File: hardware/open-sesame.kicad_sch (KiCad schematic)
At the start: 20 parts, among them J1 Barrel_Jack_Switch, J2 Screw_Terminal_01x02, J3 Screw_Terminal_01x04, J4 Screw_Terminal_01x03, J5 Screw_Terminal_01x03, J6 Qwiic_RA, U1 PC817, U2 PC817

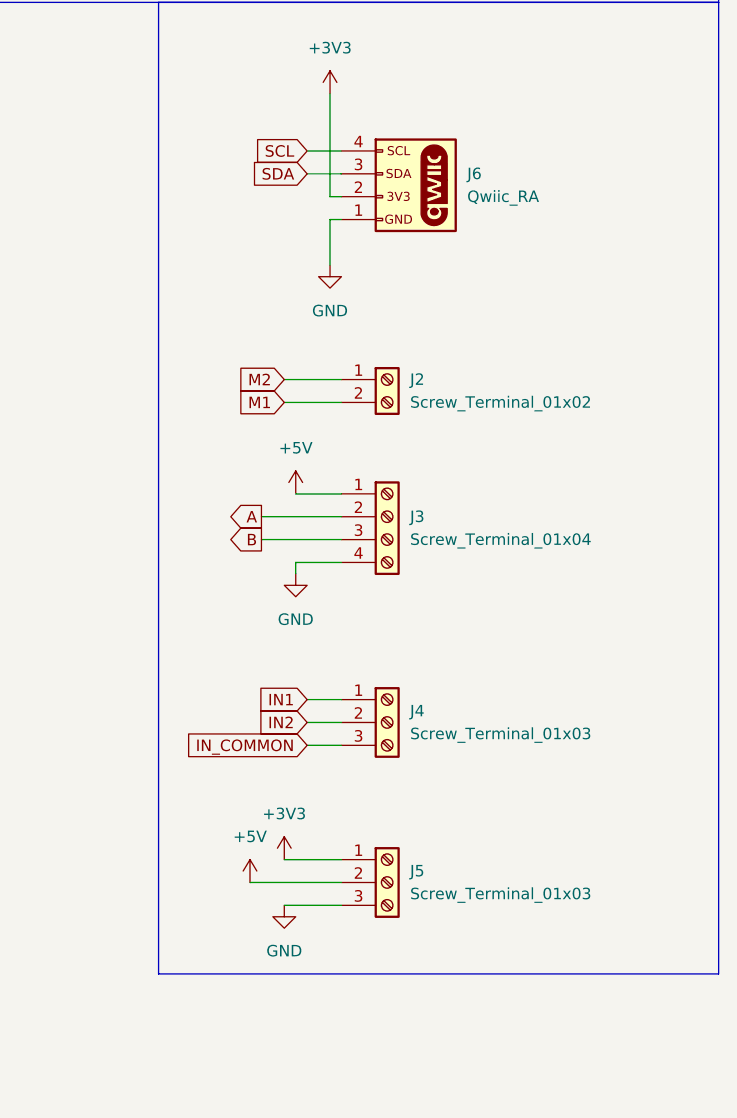
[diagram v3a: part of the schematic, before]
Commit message: Use 2x 6 port connectors
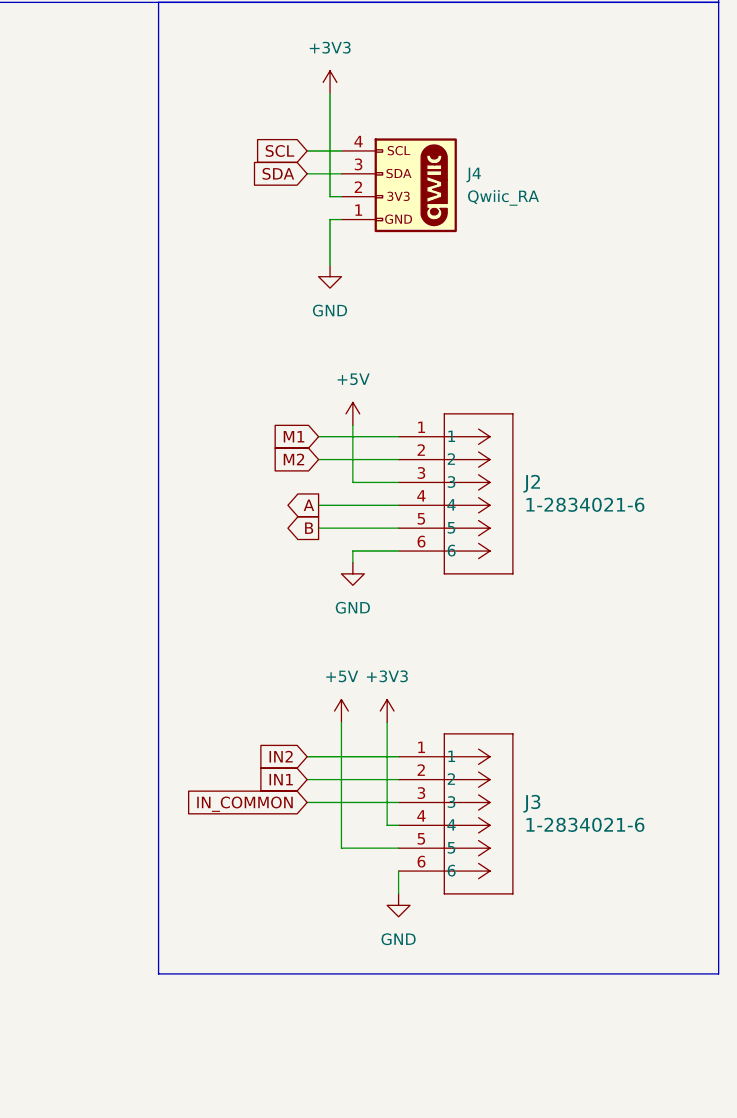
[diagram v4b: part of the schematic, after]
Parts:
- removed J2: Screw_Terminal_01x02, MyLibrary:TE_282834-2, symbol Connector:Screw_Terminal_01x02
- removed J3: Screw_Terminal_01x04, MyLibrary:TE_282834-4, symbol Connector:Screw_Terminal_01x04
- removed J4, J5: Screw_Terminal_01x03, MyLibrary:TE_282834-3, symbol Connector:Screw_Terminal_01x03
- added J2, J3: 1-2834021-6, CONN6_1-2834021-6_TEC, symbol TE-Connectivity-Connectors:1-2834021-6
- renumbered J6 to J4
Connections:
- net +3V3: now also J3.4
- net +5V: now also J2.3, J3.5
- net A: now also J2.4
- net B: now also J2.5
- net GND: now also J2.6, J3.6
- net IN1: now also J3.2
- net IN2: now also J3.1
- net IN_COMMON: now also J3.3
- net M1: now also J2.1
- net M2: now also J2.2

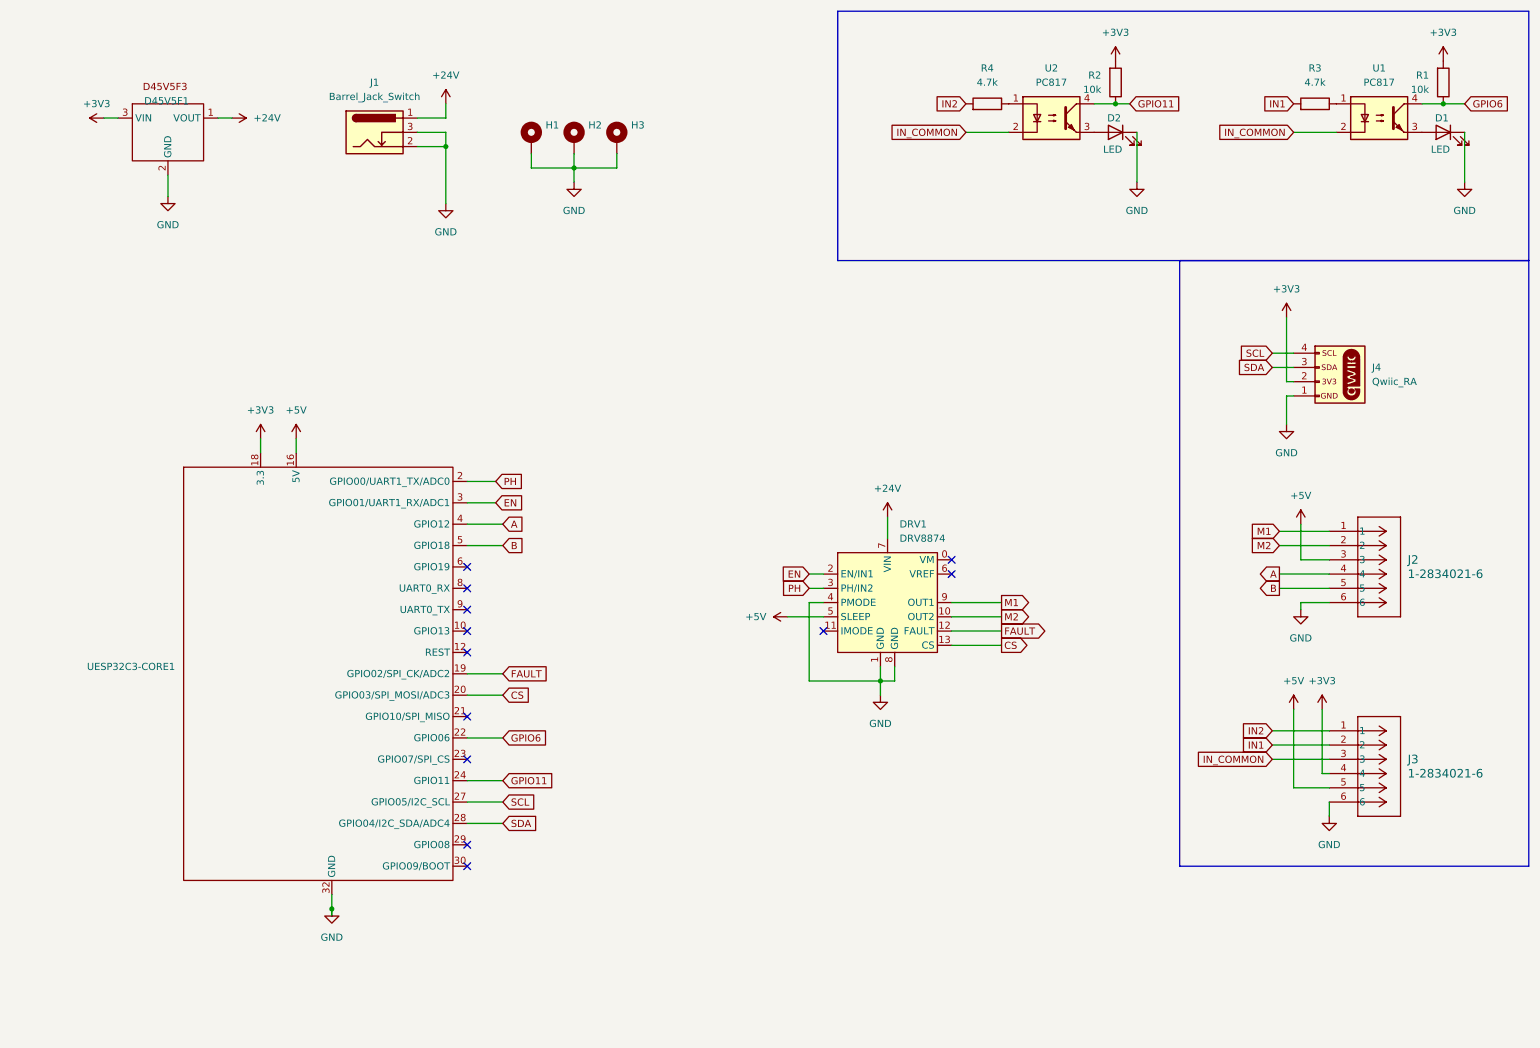
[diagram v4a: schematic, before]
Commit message: hardware: Use ESP32S3 for PCNT,
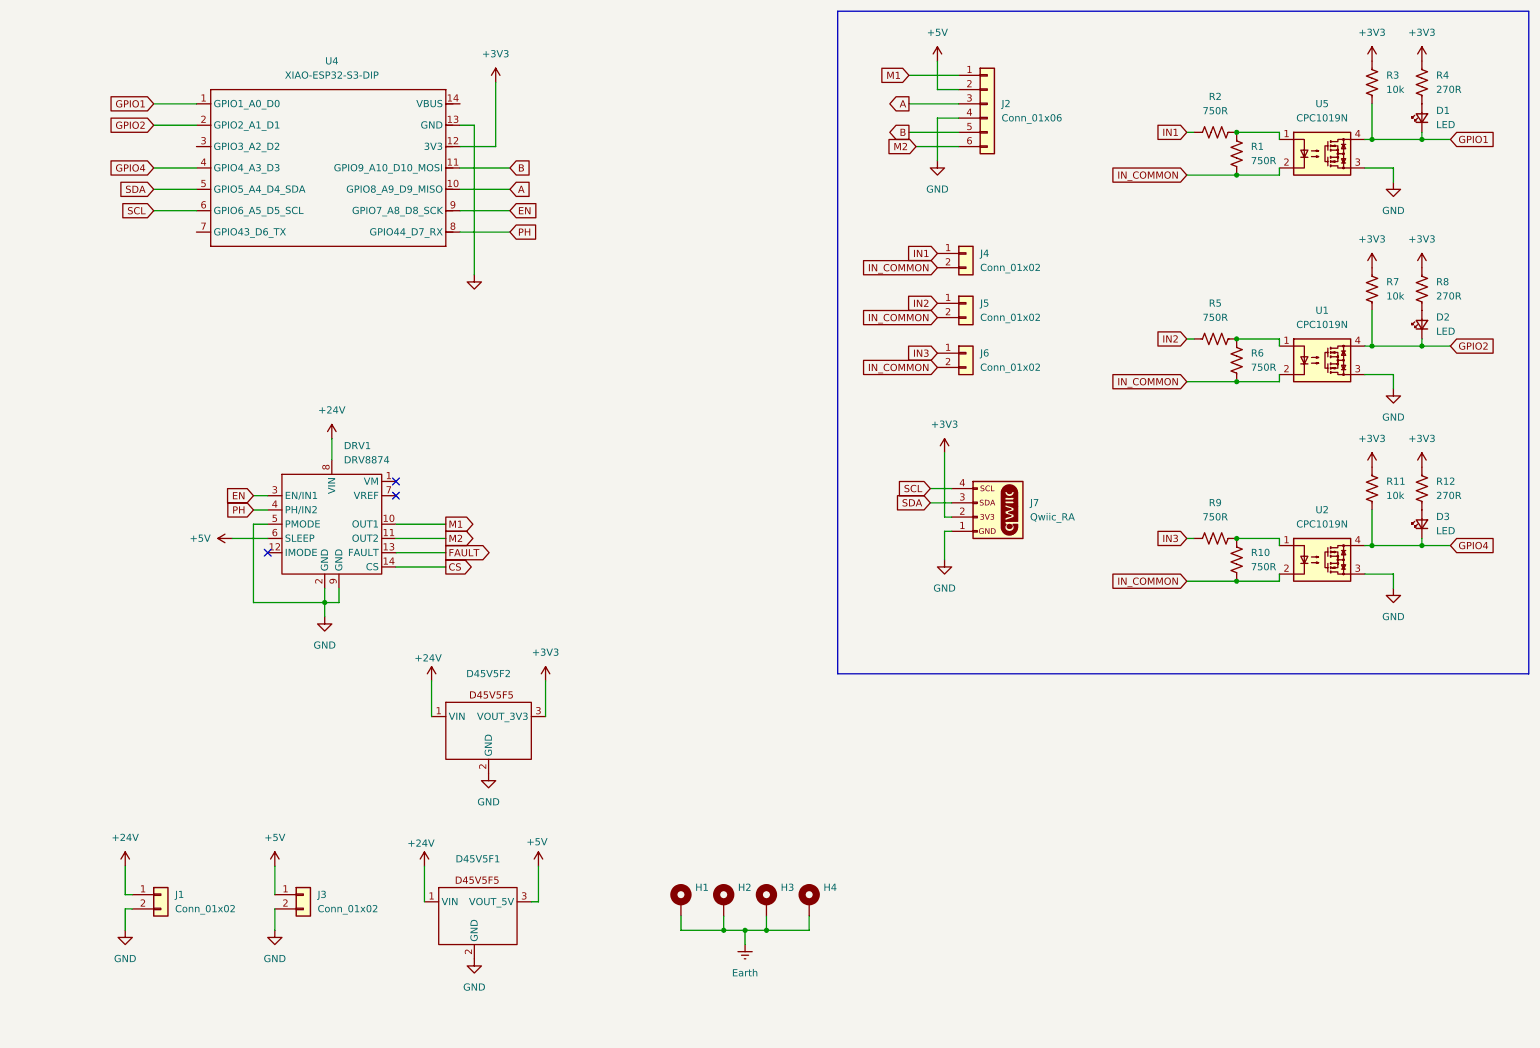
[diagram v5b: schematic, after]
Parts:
- removed D1, D2: LED, LED_SMD:LED_0603_1608Metric, symbol Device:LED
- removed D45V5F1: D45V5F3, MyLibrary:D45V5Fx, symbol MyLibrary:D45V5F3
- removed J1: Barrel_Jack_Switch, Connector_BarrelJack:BarrelJack_Horizontal, symbol Connector:Barrel_Jack_Switch
- removed J2, J3: 1-2834021-6, CONN6_1-2834021-6_TEC, symbol TE-Connectivity-Connectors:1-2834021-6
- removed R1, R2: 10k, Resistor_SMD:R_0603_1608Metric, symbol Device:R
- removed R3, R4: 4.7k, Resistor_SMD:R_0603_1608Metric, symbol Device:R
- removed U1, U2: PC817, Package_DIP:DIP-4_W7.62mm, symbol Isolator:PC817
- removed UESP32C3-CORE1: ~, MyLibrary:LUATOS_ESP32C3, symbol MyLibrary:LUATOS_ESP32C3
- added D1, D2, D3: LED, SparkFun-LED:LED_0603_1608Metric, symbol SparkFun-LED:LED
- added D45V5F1: D45V5F5, MyLibrary:D45V5Fx, symbol MyLibrary:D45V5F5
- added D45V5F2: D45V5F3, MyLibrary:D45V5Fx, symbol MyLibrary:D45V5F3
- added H4: MountingHole_Pad, MountingHole:MountingHole_2.5mm_Pad_Via, symbol Mechanical:MountingHole_Pad
- added J1, J3, J4, J5, J6: Conn_01x02, Connector_Molex:Molex_Nano-Fit_105313-xx02_1x02_P2.50mm_Horizontal, symbol Connector_Generic:Conn_01x02
- added J2: Conn_01x06, Connector_Molex:Molex_Nano-Fit_105313-xx06_1x06_P2.50mm_Horizontal, symbol Connector_Generic:Conn_01x06
- added R1, R10, R2, R5, R6, R9: 750R, Resistor_SMD:R_0603_1608Metric, symbol Device:R_US
- added R11, R3, R7: 10k, Resistor_SMD:R_0603_1608Metric, symbol Device:R_US
- added R12, R4, R8: 270R, Resistor_SMD:R_0603_1608Metric, symbol Device:R_US
- added U1, U2, U5: CPC1019N, Package_SO:SOP-4_3.8x4.1mm_P2.54mm, symbol Relay_SolidState:CPC1019N
- added U4: XIAO-ESP32-S3-DIP, XIAO_Series_Footprints:XIAO-ESP32-S3-DIP, symbol Seeed_Studio_XIAO_Series:XIAO-ESP32-S3-DIP
- H1, H2, H3: footprint MountingHole:MountingHole_3.2mm_M3_ISO7380_Pad -> MountingHole:MountingHole_2.5mm_Pad_Via
- renumbered J4 to J7
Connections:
- net +24V: now also DRV1.8 (VIN), D45V5F1.1 (VIN), D45V5F2.1 (VIN), J1.1 (Pin_1); no longer DRV1.7 (VIN)
- net +3V3: now also D45V5F2.3 (VOUT_3V3), R11.1, R12.1, R3.1, R4.1, R7.1, R8.1, U4.12 (3V3)
- net +5V: now also DRV1.6 (SLEEP), D45V5F1.3 (VOUT_5V), J2.2 (Pin_2), J3.1 (Pin_1); no longer DRV1.5 (SLEEP)
- net A: now also J2.3 (Pin_3), U4.10 (GPIO8_A9_D9_MISO)
- net B: now also J2.5 (Pin_5), U4.11 (GPIO9_A10_D10_MOSI)
- net CS: now also DRV1.14 (CS); no longer DRV1.13 (CS)
- net EN: now also DRV1.3 (EN/IN1), U4.9 (GPIO7_A8_D8_SCK); no longer DRV1.2 (EN/IN1)
- net FAULT: now also DRV1.13 (FAULT); no longer DRV1.12 (FAULT)
- net GND: now also DRV1.2 (GND), DRV1.5 (PMODE), DRV1.9 (GND), D45V5F1.2 (GND), D45V5F2.2 (GND), J1.2 (Pin_2), J2.4 (Pin_4), J3.2 (Pin_2), U1.3, U2.3, U4.13 (GND), U5.3; no longer DRV1.1 (GND), DRV1.4 (PMODE), DRV1.8 (GND), H1.1, H2.1, H3.1
- net IN1: now also J4.1 (Pin_1), R2.1
- net IN2: now also J5.1 (Pin_1), R5.1
- net IN_COMMON: now also J4.2 (Pin_2), J5.2 (Pin_2), J6.2 (Pin_2), R1.2, R10.2, R6.2, U1.2, U2.2, U5.2
- net M1: now also DRV1.10 (OUT1), J2.1 (Pin_1); no longer DRV1.9 (OUT1)
- net M2: now also DRV1.11 (OUT2), J2.6 (Pin_6); no longer DRV1.10 (OUT2)
- net PH: now also DRV1.4 (PH/IN2), U4.8 (GPIO44_D7_RX); no longer DRV1.3 (PH/IN2)
- net SCL: now also U4.6 (GPIO6_A5_D5_SCL)
- net SDA: now also U4.5 (GPIO5_A4_D4_SDA)
- new net: R10.1, R9.2, U2.1
- new net: D2.2 (A), R8.2
- new net: D1.2 (A), R4.2
- new net: R1.1, R2.2, U5.1
- new net: R5.2, R6.1, U1.1
- new net: D3.2 (A), R12.2
- new net Earth: H1.1, H2.1, H3.1, H4.1
- new net GPIO1: D1.1 (K), R3.2, U4.1 (GPIO1_A0_D0), U5.4
- new net GPIO2: D2.1 (K), R7.2, U1.4, U4.2 (GPIO2_A1_D1)
- new net GPIO4: D3.1 (K), R11.2, U2.4, U4.4 (GPIO4_A3_D3)
- new net IN3: J6.1 (Pin_1), R9.1
- no-connect marks 12 -> 3
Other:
- moved on the sheet: H1, H2, H3, J7

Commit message: hardware: shrunk board
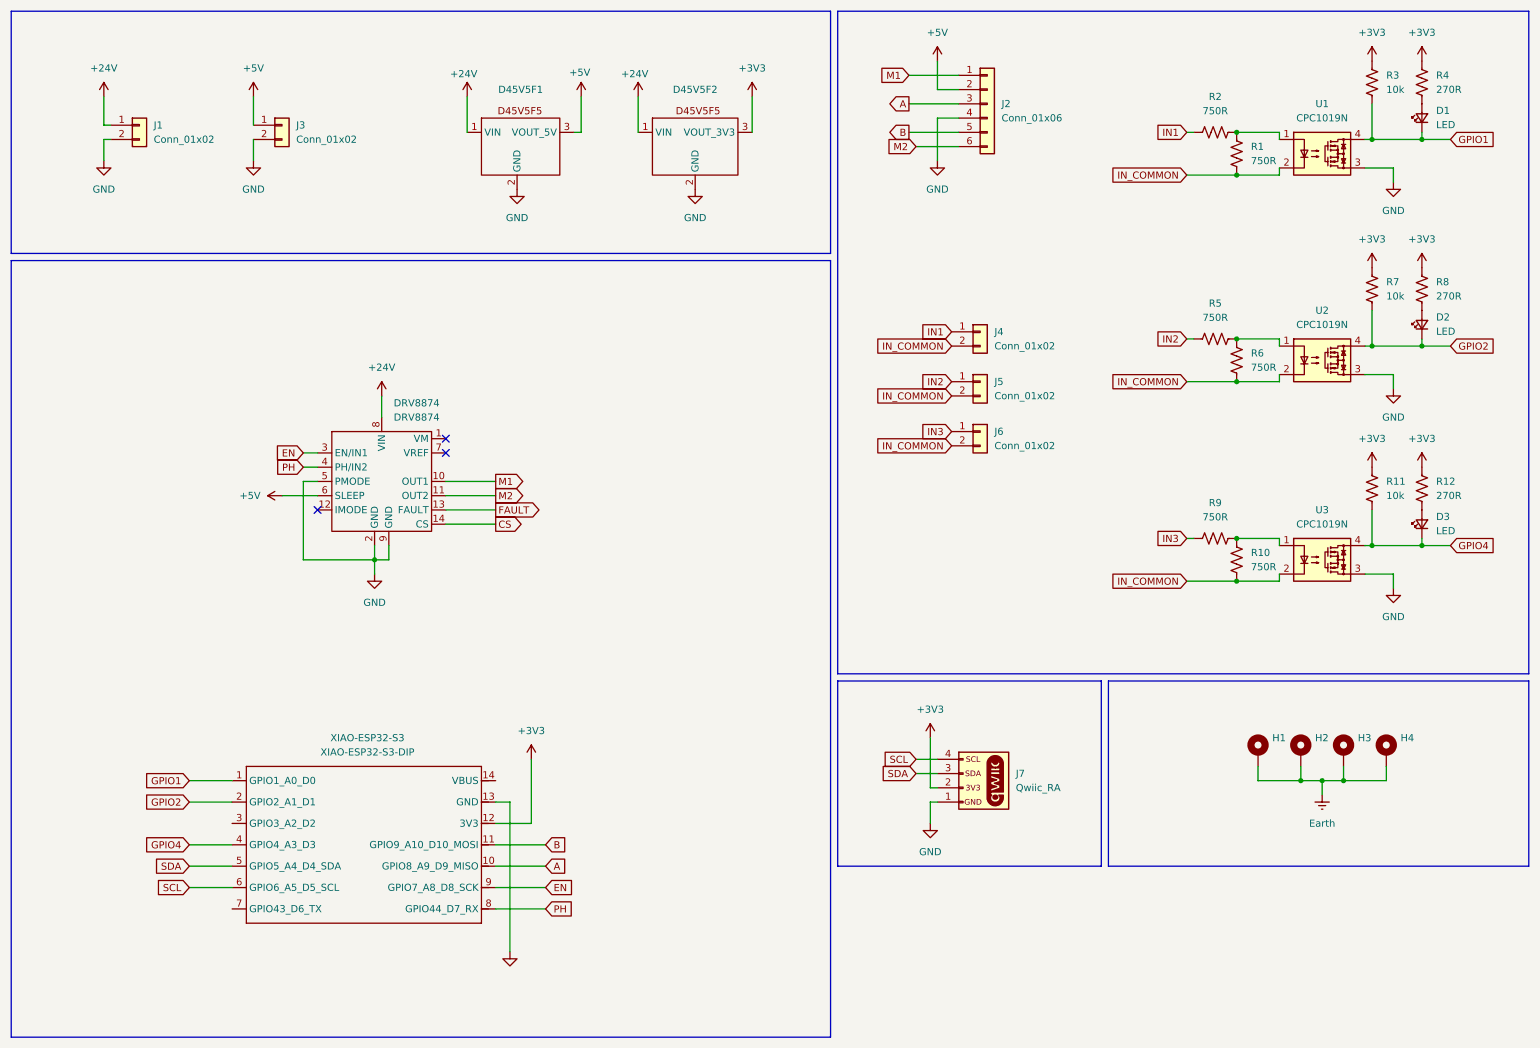
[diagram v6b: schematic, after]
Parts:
- removed U5: CPC1019N, Package_SO:SOP-4_3.8x4.1mm_P2.54mm, symbol Relay_SolidState:CPC1019N
- added U3: CPC1019N, Package_SO:SOP-4_3.8x4.1mm_P2.54mm, symbol Relay_SolidState:CPC1019N
- renumbered DRV1 to DRV8874, U4 to XIAO-ESP32-S3
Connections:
- net GND: now also U3.3
- net GPIO1: now also U1.4
- net GPIO2: now also U2.4; no longer U1.4
- net GPIO4: now also U3.4; no longer U2.4
- net IN_COMMON: now also U3.2
- net at R10.1, R9.2: now also U3.1; no longer U2.1
- net at R1.1, R2.2: now also U1.1
- net at R5.2, R6.1: now also U2.1; no longer U1.1
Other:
- moved on the sheet: D45V5F1, D45V5F2, DRV8874, H1, H2, H3, H4, J1, J3, J4, J5, J6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
